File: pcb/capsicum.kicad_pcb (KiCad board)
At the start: 2 copper layers, 70 x 55 mm, 79 parts, among them J2 Screw terminal, J3 USB-C 16+8 USB 2.0, Q1 NS2101P, Q2 BC817, SW1 SW_SPDT, SW3 SW_SPDT, U1 ESP32-C3-WROOM-02, U2 TQ33E-1, U3 AP2112K, U4 MCP73831

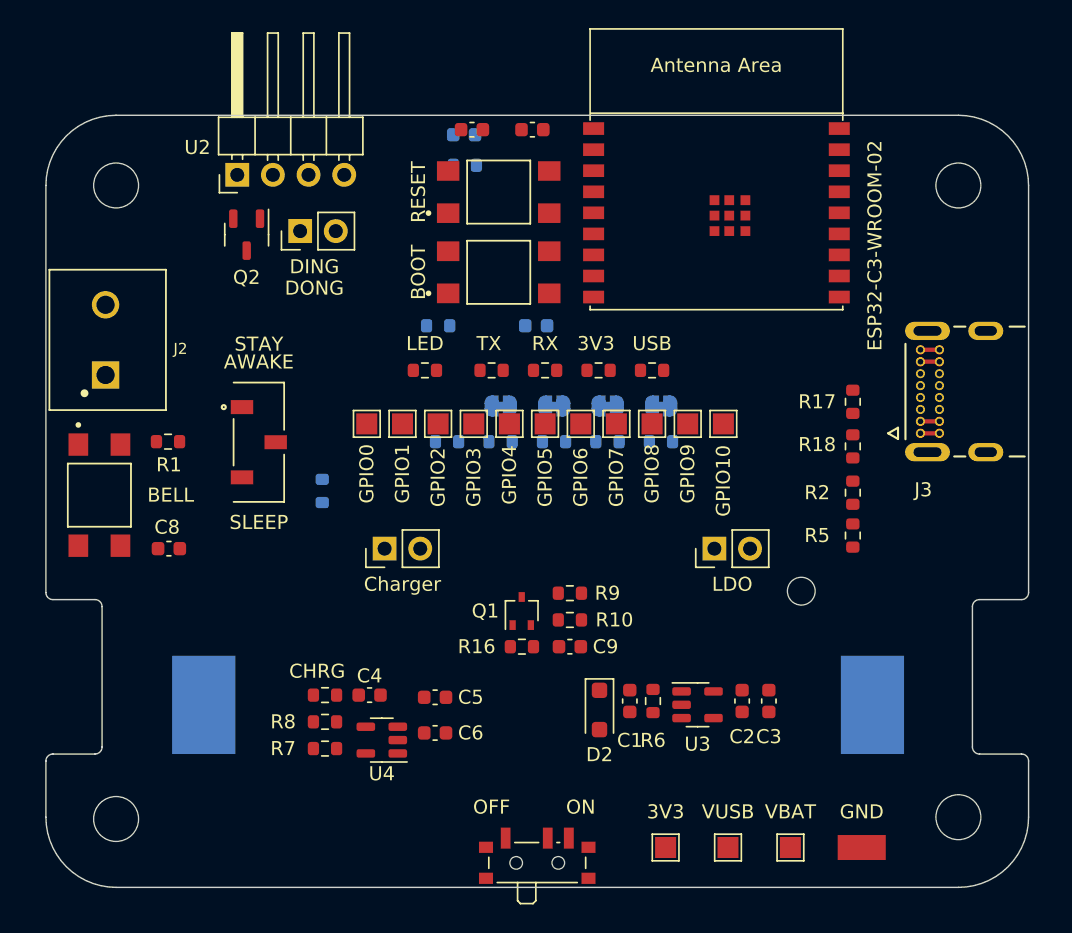
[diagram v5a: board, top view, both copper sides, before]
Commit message: feat: drop power fill zones on top and bottom layers [119 unconnected]
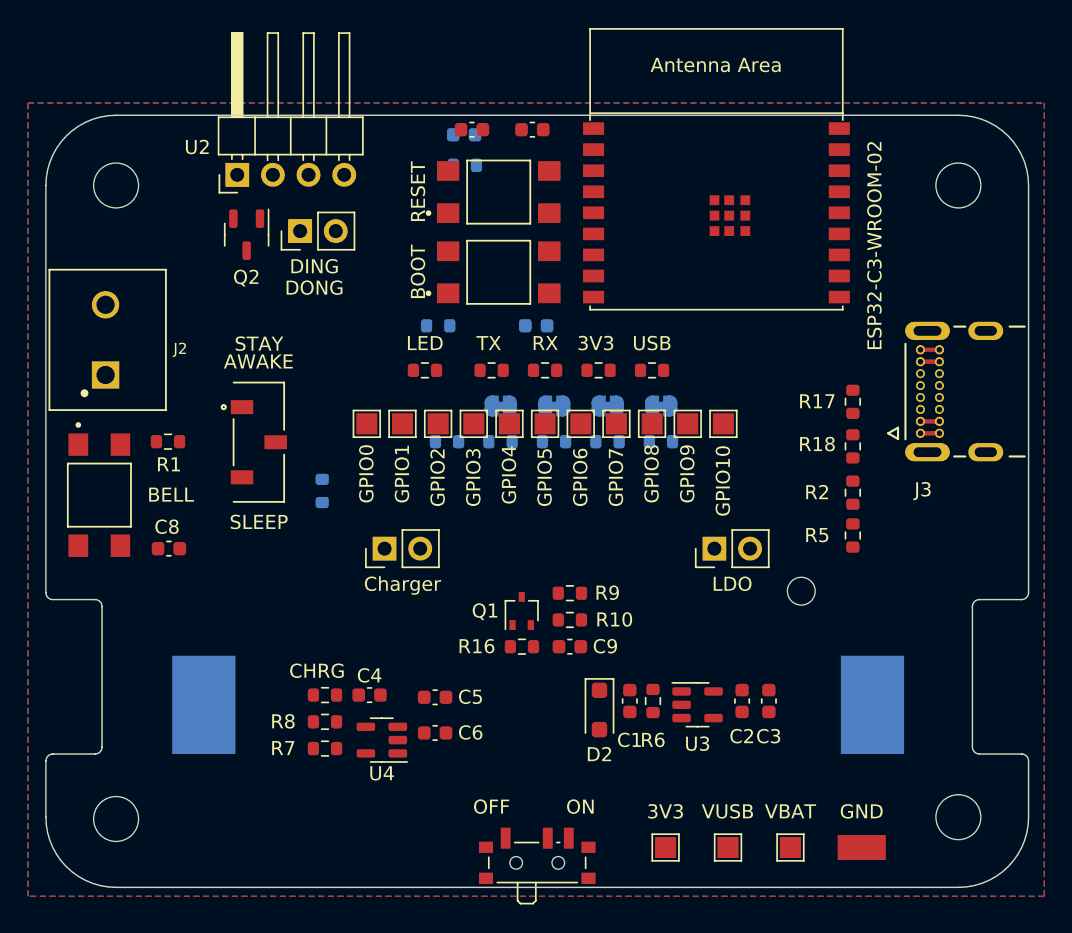
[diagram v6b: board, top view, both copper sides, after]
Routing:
- added copper zone on F.Cu, net +3V3
- added copper zone on B.Cu, net GND
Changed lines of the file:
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@@
   (title_block
     (title "Capsicum")
-    (date "2024-01-30")
+    (date "2024-01-31")
     (comment 1 "Authored by: Sayanee Basu")
     (comment 2 "Project website: https://hutscape.com/capsicum")
@@
     (style (thickness 0.15) (arrow_length 1.27) (text_position_mode 0) (extension_height 0.58642) (extension_offset 0.5) keep_text_aligned)
   )
+  (zone (net 10) (net_name "+3V3") (layer "F.Cu") (hatch edge 0.5)
+    (connect_pads (clearance 0.5))
+    (min_thickness 0.25) (filled_areas_thickness no)
+    (fill yes (thermal_gap 0.5) (thermal_bridge_width 0.5))
+    (polygon
+      (pts
+        (xy 98.73 84.12)
+        (xy 171.12 84.12)
+        (xy 171.12 140.635)
+        (xy 98.73 140.635)
+      )
+    )
+  )
+  (zone (net 2) (net_name "GND") (layer "B.Cu") (hatch edge 0.5)
+    (priority 1)
+    (connect_pads (clearance 0.5))
+    (min_thickness 0.25) (filled_areas_thickness no)
+    (fill yes (thermal_gap 0.5) (thermal_bridge_width 0.5))
+    (polygon
+      (pts
+        (xy 98.73 84.12)
+        (xy 171.12 84.12)
+        (xy 171.12 140.635)
+        (xy 98.73 140.635)
+      )
+    )
+  )
 )

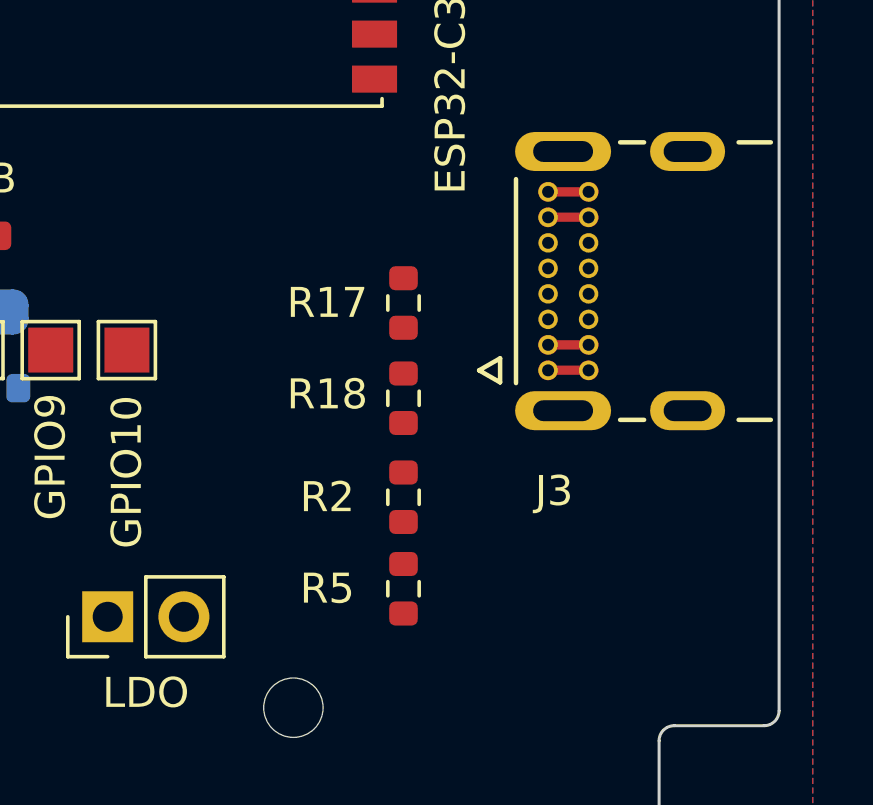
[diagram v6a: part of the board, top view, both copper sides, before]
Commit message: fix: connect USB-C A5 to resistor and ground [114 unconnected]
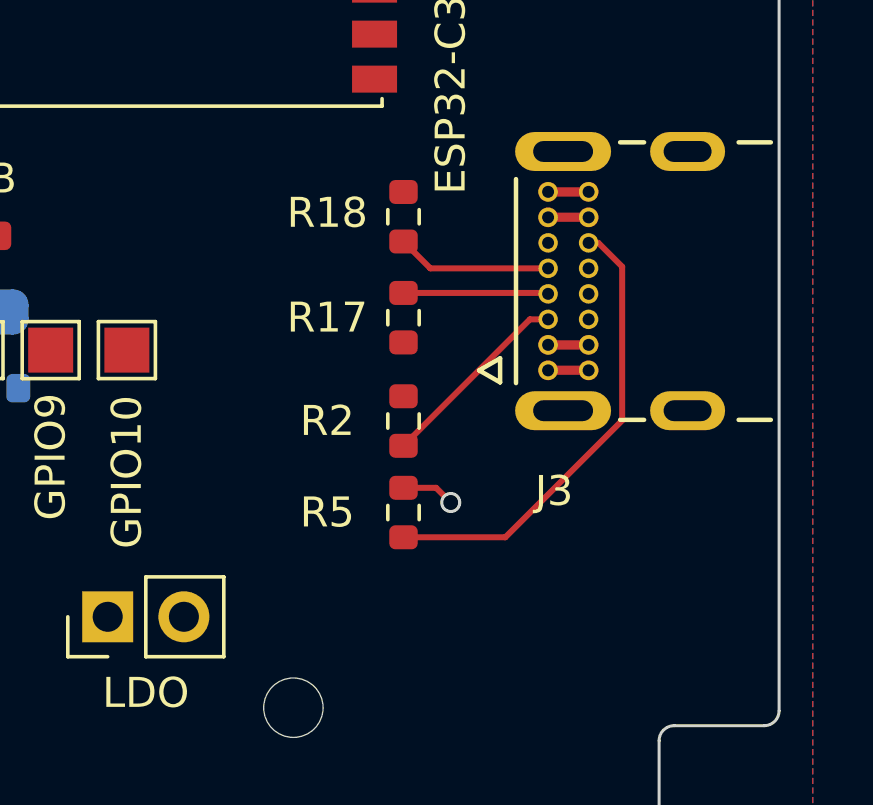
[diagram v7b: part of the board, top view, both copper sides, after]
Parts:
- moved R18 6.05 mm to (157.5, 102.5)
- moved R2 2.54 mm to (157.5, 109.3)
- moved R5 2.54 mm to (157.5, 112.4)
- moved R17 0.49 mm to (157.5, 105.9)
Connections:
- R2 pad 1: Net-(J3-CC2) -> GND
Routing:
- net Net-(J3-CC2): track 0.00 -> 15.5 mm
- net Net-(J3-CC1): track 0.00 -> 6.57 mm
- net /D-: track 0.00 -> 5.19 mm
- net /D+: track 0.00 -> 4.83 mm
- net GND: track 0.00 -> 1.78 mm, vias 0 -> 1
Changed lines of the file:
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@@
   )
   (footprint "Resistor_SMD:R_0603_1608Metric" (layer "F.Cu")
-    (at 157.48 114.935 90)
+    (at 157.48 112.395 90)
     (descr "Resistor SMD 0603 (1608 Metric), square (rectangular) end terminal, IPC_7351 nominal, (Body size source: IPC-SM-782 page 72, https://www.pcb-3d.com/wordpress/wp-content/uploads/ipc-sm-782a_amendment_1_and_2.pdf), generated with kicad-footprint-generator")
     (tags "resistor")
@@
     (property "Category" "Electronics")
     (property "DNP" "")
-    (property "Link" "https://www.pcbway.com/components/detail/CUS12TB/705754/")
-    (property "MANUFACTURER" "Nidec Copal")
-    (property "MPN" "CUS-12TB")
+    (property "Link" "https://www.pcbway.com/components/detail/JS102011JCQN/676968/")
+    (property "MANUFACTURER" "C&K")
+    (property "MPN" "JS102011JCQN")
     (property "Package" "SMD")
     (property "Sheetfile" "capsicum.kicad_sch")
     (property "Sheetname" "")
-    (property "Unit Price (USD)" "0.8033")
+    (property "Unit Price (USD)" "0.7125")
     (property "Vendor" "PCBWay")
     (property "ki_description" "Switch, single pole double throw")
@@
   )
   (footprint "Resistor_SMD:R_0603_1608Metric" (layer "F.Cu")
-    (at 157.48 111.885 -90)
+    (at 157.48 109.345 -90)
     (descr "Resistor SMD 0603 (1608 Metric), square (rectangular) end terminal, IPC_7351 nominal, (Body size source: IPC-SM-782 page 72, https://www.pcb-3d.com/wordpress/wp-content/uploads/ipc-sm-782a_amendment_1_and_2.pdf), generated with kicad-footprint-generator")
     (tags "resistor")
@@
       (stroke (width 0.1) (type solid)) (layer "F.Fab"))
     (pad "1" smd roundrect (at -0.825 0 270) (size 0.8 0.95) (layers "F.Cu" "F.Paste" "F.Mask") (roundrect_rratio 0.25)
-      (net 28 "Net-(J3-CC2)") (pintype "passive"))
+      (net 2 "GND") (pintype "passive"))
     (pad "2" smd roundrect (at 0.825 0 270) (size 0.8 0.95) (layers "F.Cu" "F.Paste" "F.Mask") (roundrect_rratio 0.25)
       (net 23 "Net-(J3-CC1)") (pintype "passive"))
@@
   )
   (footprint "Resistor_SMD:R_0603_1608Metric" (layer "F.Cu")
-    (at 157.48 105.41 90)
+    (at 157.48 105.9 90)
     (descr "Resistor SMD 0603 (1608 Metric), square (rectangular) end terminal, IPC_7351 nominal, (Body size source: IPC-SM-782 page 72, https://www.pcb-3d.com/wordpress/wp-content/uploads/ipc-sm-782a_amendment_1_and_2.pdf), generated with kicad-footprint-generator")
     (tags "resistor")
@@
   )
   (footprint "Resistor_SMD:R_0603_1608Metric" (layer "F.Cu")
-    (at 157.48 108.585 90)
+    (at 157.48 102.535 90)
     (descr "Resistor SMD 0603 (1608 Metric), square (rectangular) end terminal, IPC_7351 nominal, (Body size source: IPC-SM-782 page 72, https://www.pcb-3d.com/wordpress/wp-content/uploads/ipc-sm-782a_amendment_1_and_2.pdf), generated with kicad-footprint-generator")
     (tags "resistor")
@@
     (style (thickness 0.15) (arrow_length 1.27) (text_position_mode 0) (extension_height 0.58642) (extension_offset 0.5) keep_text_aligned)
   )
+  (segment (start 157.48 111.57) (end 158.565 111.57) (width 0.2) (layer "F.Cu") (net 2))
+  (segment (start 158.565 111.57) (end 159.055 112.06) (width 0.2) (layer "F.Cu") (net 2))
+  (via (at 159.055 112.06) (size 0.7) (drill 0.5) (layers "F.Cu" "B.Cu") (net 2))
+  (segment (start 157.48 110.17) (end 161.695 105.955) (width 0.2) (layer "F.Cu") (net 23))
+  (segment (start 161.695 105.955) (end 162.3 105.955) (width 0.2) (layer "F.Cu") (net 23))
+  (segment (start 157.48 105.075) (end 162.27 105.075) (width 0.2) (layer "F.Cu") (net 25))
+  (segment (start 162.27 105.075) (end 162.3 105.105) (width 0.2) (layer "F.Cu") (net 25))
+  (segment (start 164.77 104.201) (end 163.974 103.405) (width 0.2) (layer "F.Cu") (net 28))
+  (segment (start 163.974 103.405) (end 163.65 103.405) (width 0.2) (layer "F.Cu") (net 28))
+  (segment (start 157.48 113.22) (end 160.873051 113.22) (width 0.2) (layer "F.Cu") (net 28))
+  (segment (start 164.77 109.323051) (end 164.77 104.201) (width 0.2) (layer "F.Cu") (net 28))
+  (segment (start 160.873051 113.22) (end 164.77 109.323051) (width 0.2) (layer "F.Cu") (net 28))
+  (segment (start 158.375 104.255) (end 162.3 104.255) (width 0.2) (layer "F.Cu") (net 49))
+  (segment (start 157.48 103.36) (end 158.375 104.255) (width 0.2) (layer "F.Cu") (net 49))
   (zone (net 10) (net_name "+3V3") (layer "F.Cu") (hatch edge 0.5)
     (connect_pads (clearance 0.5))

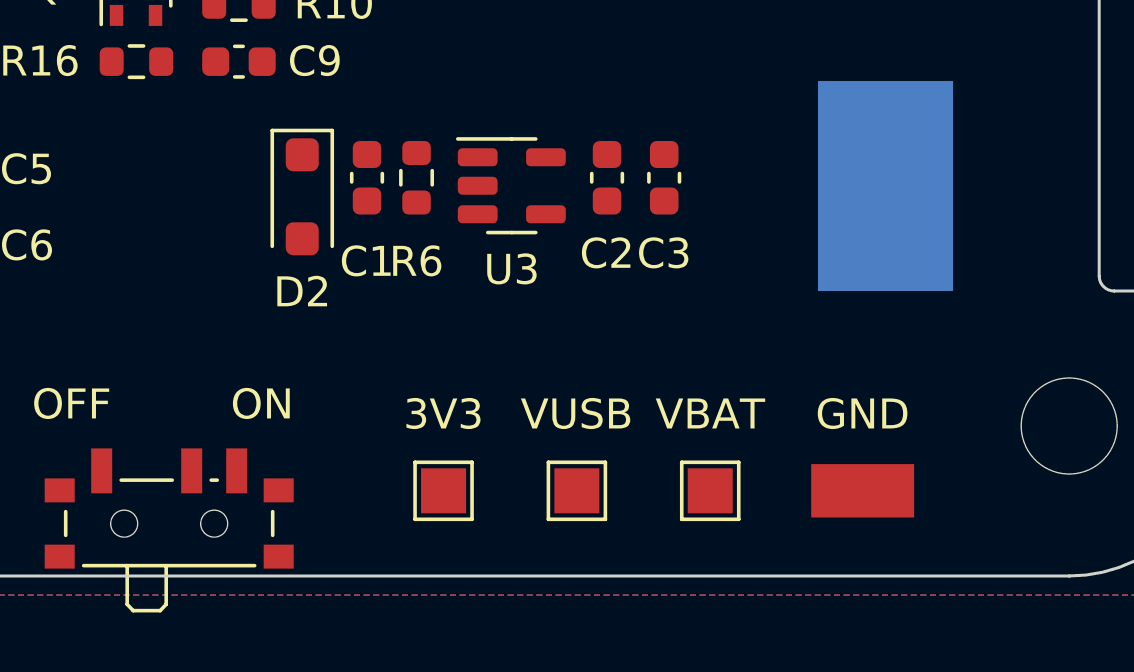
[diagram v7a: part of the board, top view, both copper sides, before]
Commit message: feat: add traces to battery logic block [110 unconected]
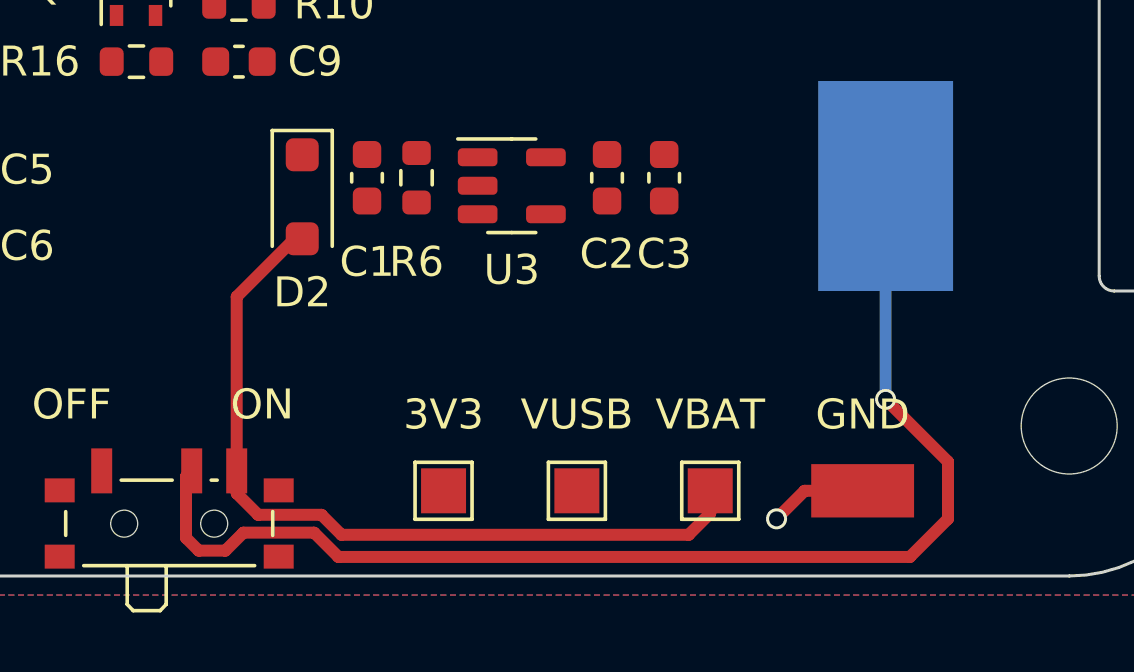
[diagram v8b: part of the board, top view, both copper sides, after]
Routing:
- net Net-(BT1-+): track 0.00 -> 41.2 mm, vias 0 -> 1
- net /VBAT: track 0.00 -> 26.9 mm
- net GND: track 1.78 -> 5.04 mm, vias 1 -> 2
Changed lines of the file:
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@@
     (style (thickness 0.15) (arrow_length 1.27) (text_position_mode 0) (extension_height 0.58642) (extension_offset 0.5) keep_text_aligned)
   )
+  (segment (start 135.56 136.685) (end 135.75 136.495) (width 0.4) (layer "F.Cu") (net 1))
+  (segment (start 136.872792 139.155) (end 135.985 139.155) (width 0.4) (layer "F.Cu") (net 1))
+  (segment (start 160.96 138.095) (end 159.69 139.365) (width 0.4) (layer "F.Cu") (net 1))
+  (segment (start 135.985 139.155) (end 135.56 138.73) (width 0.4) (layer "F.Cu") (net 1))
+  (segment (start 140.64 139.365) (end 139.83 138.555) (width 0.4) (layer "F.Cu") (net 1))
+  (segment (start 158.88 134.11) (end 160.96 136.19) (width 0.4) (layer "F.Cu") (net 1))
+  (segment (start 160.96 136.19) (end 160.96 138.095) (width 0.4) (layer "F.Cu") (net 1))
+  (segment (start 135.56 138.73) (end 135.56 136.685) (width 0.4) (layer "F.Cu") (net 1))
+  (segment (start 137.472792 138.555) (end 136.872792 139.155) (width 0.4) (layer "F.Cu") (net 1))
+  (segment (start 139.83 138.555) (end 137.472792 138.555) (width 0.4) (layer "F.Cu") (net 1))
+  (segment (start 159.69 139.365) (end 140.64 139.365) (width 0.4) (layer "F.Cu") (net 1))
+  (via (at 158.88 134.11) (size 0.7) (drill 0.5) (layers "F.Cu" "B.Cu") (net 1))
+  (segment (start 159.055 134.285) (end 158.88 134.11) (width 0.4) (layer "B.Cu") (net 1))
+  (segment (start 158.88 127) (end 158.88 134.11) (width 0.4) (layer "B.Cu") (net 1))
   (segment (start 157.48 111.57) (end 158.565 111.57) (width 0.2) (layer "F.Cu") (net 2))
+  (segment (start 158.115 137.16) (end 156.18 137.16) (width 0.4) (layer "F.Cu") (net 2))
   (segment (start 158.565 111.57) (end 159.055 112.06) (width 0.2) (layer "F.Cu") (net 2))
+  (segment (start 156.18 137.16) (end 155.245 138.095) (width 0.4) (layer "F.Cu") (net 2))
+  (via (at 155.245 138.095) (size 0.7) (drill 0.5) (layers "F.Cu" "B.Cu") (net 2))
   (via (at 159.055 112.06) (size 0.7) (drill 0.5) (layers "F.Cu" "B.Cu") (net 2))
+  (segment (start 137.965 137.96) (end 137.25 137.245) (width 0.4) (layer "F.Cu") (net 13))
+  (segment (start 137.25 137.245) (end 137.25 136.495) (width 0.4) (layer "F.Cu") (net 13))
+  (segment (start 137.25 130.69) (end 137.25 136.495) (width 0.4) (layer "F.Cu") (net 13))
+  (segment (start 152.318229 138.626771) (end 140.743229 138.626771) (width 0.4) (layer "F.Cu") (net 13))
+  (segment (start 139.18 128.76) (end 137.25 130.69) (width 0.4) (layer "F.Cu") (net 13))
+  (segment (start 153.035 137.16) (end 153.035 137.91) (width 0.4) (layer "F.Cu") (net 13))
+  (segment (start 140.743229 138.626771) (end 140.076457 137.96) (width 0.4) (layer "F.Cu") (net 13))
+  (segment (start 140.076457 137.96) (end 137.965 137.96) (width 0.4) (layer "F.Cu") (net 13))
+  (segment (start 139.435 128.76) (end 139.18 128.76) (width 0.4) (layer "F.Cu") (net 13))
+  (segment (start 153.035 137.91) (end 152.318229 138.626771) (width 0.4) (layer "F.Cu") (net 13))
   (segment (start 157.48 110.17) (end 161.695 105.955) (width 0.2) (layer "F.Cu") (net 23))
   (segment (start 161.695 105.955) (end 162.3 105.955) (width 0.2) (layer "F.Cu") (net 23))
